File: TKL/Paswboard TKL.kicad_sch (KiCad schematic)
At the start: 348 parts, among them SW1 SW_Push, SW10 SW_Push, SW11 SW_Push, SW12 SW_Push, SW13 SW_Push, SW14 SW_Push, SW15 SW_Push, SW16 SW_Push, SW17 SW_Push, SW18 SW_Push, SW19 SW_Push, SW2 SW_Push, SW20 SW_Push, SW21 SW_Push, SW22 SW_Push, SW23 SW_Push, SW24 SW_Push, SW25 SW_Push, SW26 SW_Push, SW27 SW_Push, SW28 SW_Push, SW29 SW_Push, SW3 SW_Push, SW30 SW_Push, SW31 SW_Push, SW32 SW_Push, SW33 SW_Push, SW34 SW_Push, SW35 SW_Push, SW36 SW_Push, SW37 SW_Push, SW38 SW_Push, SW39 SW_Push, SW4 SW_Push, SW40 SW_Push, SW41 SW_Push, SW42 SW_Push, SW43 SW_Push, SW44 SW_Push, SW45 SW_Push, SW46 SW_Push, SW47 SW_Push, SW48 SW_Push, SW49 SW_Push, SW5 SW_Push, SW50 SW_Push, SW51 SW_Push, SW52 SW_Push, SW53 SW_Push, SW54 SW_Push, SW55 SW_Push, SW56 SW_Push, SW57 SW_Push, SW58 SW_Push, SW59 SW_Push, SW6 SW_Push, SW60 SW_Push, SW61 SW_Push, SW62 SW_Push, SW63 SW_Push, SW64 SW_Push, SW65 SW_Push, SW66 SW_Push, SW67 SW_Push, SW68 SW_Push, SW69 SW_Push, SW7 SW_Push, SW70 SW_Push, SW71 SW_Push, SW72 SW_Push, SW73 SW_Push, SW74 SW_Push, SW75 SW_Push, SW76 SW_Push, SW77 SW_Push, SW78 SW_Push, SW79 SW_Push, SW8 SW_Push, SW80 SW_Push, SW81 SW_Push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

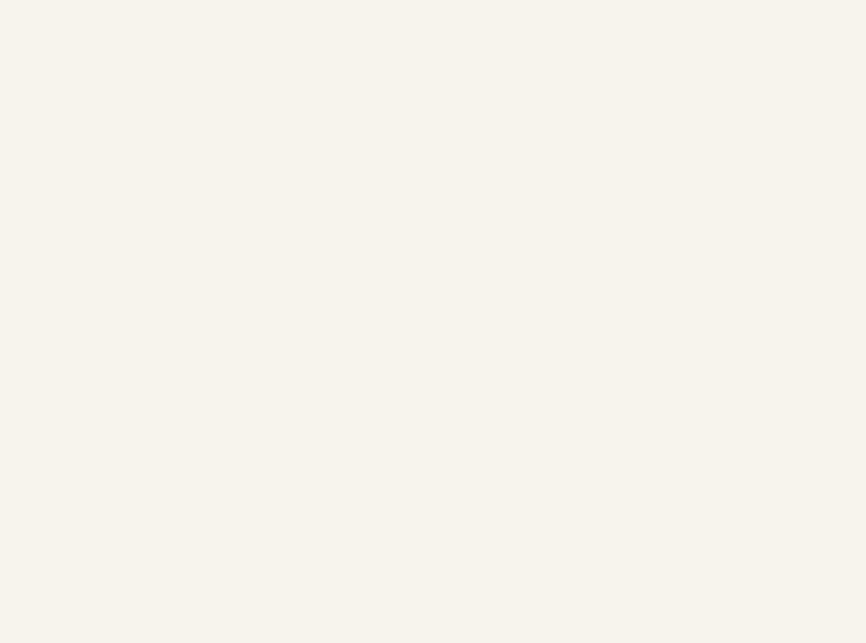
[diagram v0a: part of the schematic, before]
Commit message: adding holes and stabilisers
the "mounting holes" are actually used for holes and stablisers
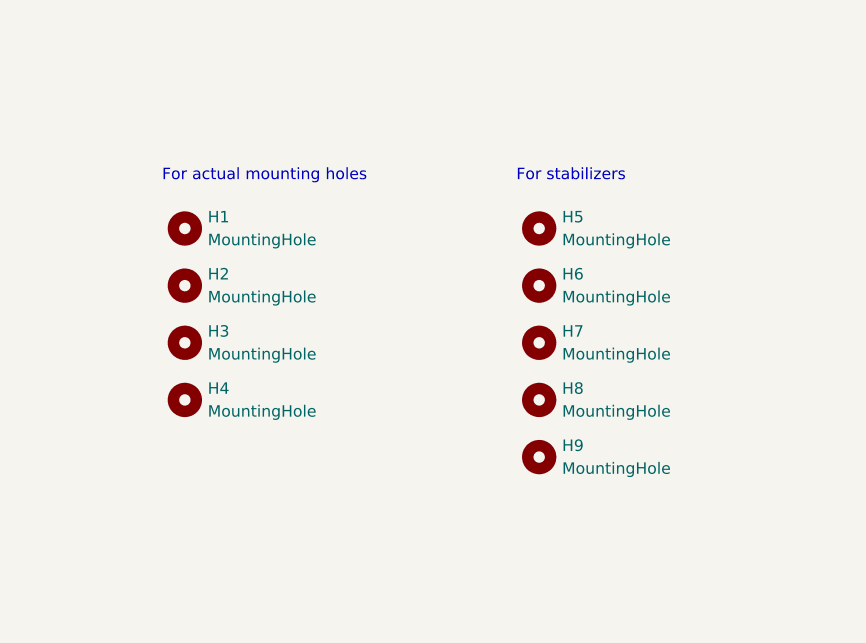
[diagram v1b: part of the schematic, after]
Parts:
- added H1, H2, H3, H4: MountingHole, MountingHole:MountingHole_3mm, symbol Mechanical:MountingHole
- added H5, H6, H7, H8: MountingHole, Mounting_Keyboard_Stabilizer:Stabilizer_Cherry_MX_2.00u, symbol Mechanical:MountingHole
- added H9: MountingHole, Mounting_Keyboard_Stabilizer:Stabilizer_Cherry_MX_6.25u, symbol Mechanical:MountingHole
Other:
- note added: "For actual mounting holes"
- note added: "For stabilizers"
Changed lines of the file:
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@@
     (stroke (width 0) (type default) (color 0 0 0 0))
   )
+  (text "For stabilizers" (at 72.39 160.02 0)
+    (effects (font (size 1.27 1.27)) (justify left bottom))
+  )
+  (text "For actual mounting holes" (at 33.02 160.02 0)
+    (effects (font (size 1.27 1.27)) (justify left bottom))
+  )
   (symbol (lib_id "Diode:1N4148") (at 114.3 401.32 0) (unit 1)
     (in_bom yes) (on_board yes) (fields_autoplaced)
@@
     (pin "4")
   )
+  (symbol (lib_id "Mechanical:MountingHole") (at 35.56 184.15 0) (unit 1)
+    (in_bom yes) (on_board yes) (fields_autoplaced)
+    (property "Reference" "H4" (id 0) (at 38.1 182.8799 0)
+      (effects (font (size 1.27 1.27)) (justify left))
+    )
+    (property "Value" "MountingHole" (id 1) (at 38.1 185.4199 0)
+      (effects (font (size 1.27 1.27)) (justify left))
+    )
+    (property "Footprint" "MountingHole:MountingHole_3mm" (id 2) (at 35.56 184.15 0)
+      (effects (font (size 1.27 1.27)) hide)
+    )
+    (property "Datasheet" "~" (id 3) (at 35.56 184.15 0)
+      (effects (font (size 1.27 1.27)) hide)
+    )
+  )
   (symbol (lib_id "LED:WS2812B") (at 243.84 97.79 0) (unit 1)
     (in_bom yes) (on_board yes) (fields_autoplaced)
@@
     (pin "2")
   )
+  (symbol (lib_id "Mechanical:MountingHole") (at 35.56 171.45 0) (unit 1)
+    (in_bom yes) (on_board yes) (fields_autoplaced)
+    (property "Reference" "H2" (id 0) (at 38.1 170.1799 0)
+      (effects (font (size 1.27 1.27)) (justify left))
+    )
+    (property "Value" "MountingHole" (id 1) (at 38.1 172.7199 0)
+      (effects (font (size 1.27 1.27)) (justify left))
+    )
+    (property "Footprint" "MountingHole:MountingHole_3mm" (id 2) (at 35.56 171.45 0)
+      (effects (font (size 1.27 1.27)) hide)
+    )
+    (property "Datasheet" "~" (id 3) (at 35.56 171.45 0)
+      (effects (font (size 1.27 1.27)) hide)
+    )
+  )
   (symbol (lib_id "LED:WS2812B") (at 354.33 44.45 0) (unit 1)
     (in_bom yes) (on_board yes) (fields_autoplaced)
@@
     (pin "4")
   )
+  (symbol (lib_id "Mechanical:MountingHole") (at 74.93 184.15 0) (unit 1)
+    (in_bom yes) (on_board yes) (fields_autoplaced)
+    (property "Reference" "H8" (id 0) (at 77.47 182.8799 0)
+      (effects (font (size 1.27 1.27)) (justify left))
+    )
+    (property "Value" "MountingHole" (id 1) (at 77.47 185.4199 0)
+      (effects (font (size 1.27 1.27)) (justify left))
+    )
+    (property "Footprint" "Mounting_Keyboard_Stabilizer:Stabilizer_Cherry_MX_2.00u" (id 2) (at 74.93 184.15 0)
+      (effects (font (size 1.27 1.27)) hide)
+    )
+    (property "Datasheet" "~" (id 3) (at 74.93 184.15 0)
+      (effects (font (size 1.27 1.27)) hide)
+    )
+  )
   (symbol (lib_id "Device:C_Polarized_Small") (at 401.32 102.87 0) (unit 1)
     (in_bom yes) (on_board yes) (fields_autoplaced)
@@
     (pin "2")
   )
+  (symbol (lib_id "Mechanical:MountingHole") (at 35.56 177.8 0) (unit 1)
+    (in_bom yes) (on_board yes) (fields_autoplaced)
+    (property "Reference" "H3" (id 0) (at 38.1 176.5299 0)
+      (effects (font (size 1.27 1.27)) (justify left))
+    )
+    (property "Value" "MountingHole" (id 1) (at 38.1 179.0699 0)
+      (effects (font (size 1.27 1.27)) (justify left))
+    )
+    (property "Footprint" "MountingHole:MountingHole_3mm" (id 2) (at 35.56 177.8 0)
+      (effects (font (size 1.27 1.27)) hide)
+    )
+    (property "Datasheet" "~" (id 3) (at 35.56 177.8 0)
+      (effects (font (size 1.27 1.27)) hide)
+    )
+  )
   (symbol (lib_id "Switch:SW_Push") (at 100.33 306.07 0) (unit 1)
     (in_bom yes) (on_board yes) (fields_autoplaced)
@@
     (pin "2")
   )
+  (symbol (lib_id "Mechanical:MountingHole") (at 74.93 171.45 0) (unit 1)
+    (in_bom yes) (on_board yes) (fields_autoplaced)
+    (property "Reference" "H6" (id 0) (at 77.47 170.1799 0)
+      (effects (font (size 1.27 1.27)) (justify left))
+    )
+    (property "Value" "MountingHole" (id 1) (at 77.47 172.7199 0)
+      (effects (font (size 1.27 1.27)) (justify left))
+    )
+    (property "Footprint" "Mounting_Keyboard_Stabilizer:Stabilizer_Cherry_MX_2.00u" (id 2) (at 74.93 171.45 0)
+      (effects (font (size 1.27 1.27)) hide)
+    )
+    (property "Datasheet" "~" (id 3) (at 74.93 171.45 0)
+      (effects (font (size 1.27 1.27)) hide)
+    )
+  )
   (symbol (lib_id "Diode:1N4148") (at 128.27 314.96 0) (unit 1)
     (in_bom yes) (on_board yes) (fields_autoplaced)
@@
     (pin "2")
   )
+  (symbol (lib_id "Mechanical:MountingHole") (at 74.93 190.5 0) (unit 1)
+    (in_bom yes) (on_board yes) (fields_autoplaced)
+    (property "Reference" "H9" (id 0) (at 77.47 189.2299 0)
+      (effects (font (size 1.27 1.27)) (justify left))
+    )
+    (property "Value" "MountingHole" (id 1) (at 77.47 191.7699 0)
+      (effects (font (size 1.27 1.27)) (justify left))
+    )
+    (property "Footprint" "Mounting_Keyboard_Stabilizer:Stabilizer_Cherry_MX_6.25u" (id 2) (at 74.93 190.5 0)
+      (effects (font (size 1.27 1.27)) hide)
+    )
+    (property "Datasheet" "~" (id 3) (at 74.93 190.5 0)
+      (effects (font (size 1.27 1.27)) hide)
+    )
+  )
   (symbol (lib_id "Diode:1N4148") (at 240.03 336.55 0) (unit 1)
     (in_bom yes) (on_board yes) (fields_autoplaced)
@@
     (pin "2")
   )
+  (symbol (lib_id "Mechanical:MountingHole") (at 74.93 165.1 0) (unit 1)
+    (in_bom yes) (on_board yes) (fields_autoplaced)
+    (property "Reference" "H5" (id 0) (at 77.47 163.8299 0)
+      (effects (font (size 1.27 1.27)) (justify left))
+    )
+    (property "Value" "MountingHole" (id 1) (at 77.47 166.3699 0)
+      (effects (font (size 1.27 1.27)) (justify left))
+    )
+    (property "Footprint" "Mounting_Keyboard_Stabilizer:Stabilizer_Cherry_MX_2.00u" (id 2) (at 74.93 165.1 0)
+      (effects (font (size 1.27 1.27)) hide)
+    )
+    (property "Datasheet" "~" (id 3) (at 74.93 165.1 0)
+      (effects (font (size 1.27 1.27)) hide)
+    )
+  )
   (symbol (lib_id "Diode:1N4148") (at 58.42 293.37 0) (unit 1)
     (in_bom yes) (on_board yes) (fields_autoplaced)
@@
     (pin "2")
   )
+  (symbol (lib_id "Mechanical:MountingHole") (at 35.56 165.1 0) (unit 1)
+    (in_bom yes) (on_board yes) (fields_autoplaced)
+    (property "Reference" "H1" (id 0) (at 38.1 163.8299 0)
+      (effects (font (size 1.27 1.27)) (justify left))
+    )
+    (property "Value" "MountingHole" (id 1) (at 38.1 166.3699 0)
+      (effects (font (size 1.27 1.27)) (justify left))
+    )
+    (property "Footprint" "MountingHole:MountingHole_3mm" (id 2) (at 35.56 165.1 0)
+      (effects (font (size 1.27 1.27)) hide)
+    )
+    (property "Datasheet" "~" (id 3) (at 35.56 165.1 0)
+      (effects (font (size 1.27 1.27)) hide)
+    )
+  )
   (symbol (lib_id "LED:WS2812B") (at 280.67 44.45 0) (unit 1)
     (in_bom yes) (on_board yes) (fields_autoplaced)
@@
     (pin "4")
   )
+  (symbol (lib_id "Mechanical:MountingHole") (at 74.93 177.8 0) (unit 1)
+    (in_bom yes) (on_board yes) (fields_autoplaced)
+    (property "Reference" "H7" (id 0) (at 77.47 176.5299 0)
+      (effects (font (size 1.27 1.27)) (justify left))
+    )
+    (property "Value" "MountingHole" (id 1) (at 77.47 179.0699 0)
+      (effects (font (size 1.27 1.27)) (justify left))
+    )
+    (property "Footprint" "Mounting_Keyboard_Stabilizer:Stabilizer_Cherry_MX_2.00u" (id 2) (at 74.93 177.8 0)
+      (effects (font (size 1.27 1.27)) hide)
+    )
+    (property "Datasheet" "~" (id 3) (at 74.93 177.8 0)
+      (effects (font (size 1.27 1.27)) hide)
+    )
+  )
   (symbol (lib_id "Diode:1N4148") (at 86.36 358.14 0) (unit 1)
     (in_bom yes) (on_board yes) (fields_autoplaced)
@@
       (reference "D174") (unit 1) (value "WS2812B") (footprint "LED_WS2812B_PLCC4_3.5x2.8mm_P1:LED_WS2812B_PLCC4_3.5x2.8mm_P1.5mm")
     )
+    (path "/e82f7475-ff3a-4f6a-a70f-473d30d0e739"
+      (reference "H1") (unit 1) (value "MountingHole") (footprint "MountingHole:MountingHole_3mm")
+    )
+    (path "/42e16f8f-8cb6-4cd7-9de8-2f3fb2a95a61"
+      (reference "H2") (unit 1) (value "MountingHole") (footprint "MountingHole:MountingHole_3mm")
+    )
+    (path "/a3bc65c7-5166-4cd5-8397-8241ca4bef3c"
+      (reference "H3") (unit 1) (value "MountingHole") (footprint "MountingHole:MountingHole_3mm")
+    )
+    (path "/1dcc875e-d923-4cf9-aa92-c7d8e0da9918"
+      (reference "H4") (unit 1) (value "MountingHole") (footprint "MountingHole:MountingHole_3mm")
+    )
+    (path "/d8565d0c-4ad2-4bf2-9e38-c6045441e4e3"
+      (reference "H5") (unit 1) (value "MountingHole") (footprint "Mounting_Keyboard_Stabilizer:Stabilizer_Cherry_MX_2.00u")
+    )
+    (path "/c3363ce8-9c85-463b-8086-af6765de43b2"
+      (reference "H6") (unit 1) (value "MountingHole") (footprint "Mounting_Keyboard_Stabilizer:Stabilizer_Cherry_MX_2.00u")
+    )
+    (path "/fc29ed75-1fee-4b18-92e2-dc1eff7191ea"
+      (reference "H7") (unit 1) (value "MountingHole") (footprint "Mounting_Keyboard_Stabilizer:Stabilizer_Cherry_MX_2.00u")
+    )
+    (path "/9c0dc6b4-586c-4962-bc27-32a7ece298ec"
+      (reference "H8") (unit 1) (value "MountingHole") (footprint "Mounting_Keyboard_Stabilizer:Stabilizer_Cherry_MX_2.00u")
+    )
+    (path "/cec8b448-9e55-4d7b-b750-45f6e04009ef"
+      (reference "H9") (unit 1) (value "MountingHole") (footprint "Mounting_Keyboard_Stabilizer:Stabilizer_Cherry_MX_6.25u")
+    )
     (path "/2c4acb85-c980-4916-a63d-02c86003fa59"

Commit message: starting over
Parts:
- D100, D101, D102, D103, D104, D105, D106, D107, D108, D109, D110, D111, D112, D113, D114, D115, D116, D117, D118, D119, D120, D121, D122, D123, D124, D125, D126, D127, D128, D129, D130, D131, D132, D133, D134, D135, D136, D137, D138, D139, D140, D141, D142, D143, D144, D145, D146, D147, D148, D149, D150, D151, D152, D153, D154, D155, D156, D157, D158, D159, D160, D161, D162, D163, D164, D165, D166, D167, D168, D169, D170, D171, D172, D173, D174, D88, D89, D90, D91, D92, D93, D94, D95, D96, D97, D98, D99: footprint LED_WS2812B_PLCC4_3.5x2.8mm_P1:LED_WS2812B_PLCC4_3.5x2.8mm_P1.5mm -> footprints:LED_WS2812B_3.5x2.8_C2890364
